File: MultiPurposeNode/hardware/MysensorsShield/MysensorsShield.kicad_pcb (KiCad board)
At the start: 2 copper layers, 20 parts, among them J1 IR RECEIVER, J2 TEMP SENSOR, J3 RADIO1, J4 RADIO2, J5 STEMMA, Q1 2N3904, U1 NRF24L01_Breakout

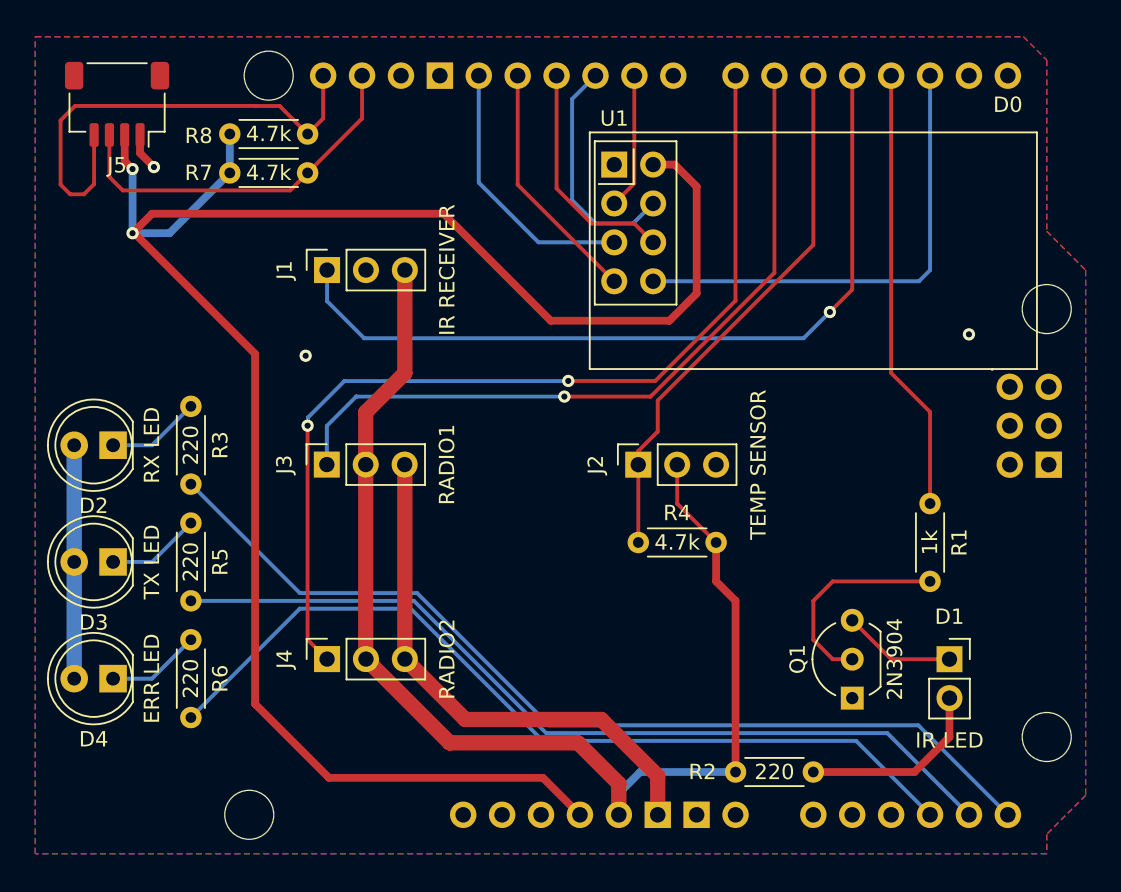
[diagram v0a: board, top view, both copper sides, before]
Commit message: MultiPurposeNode Rev.1 shield complete
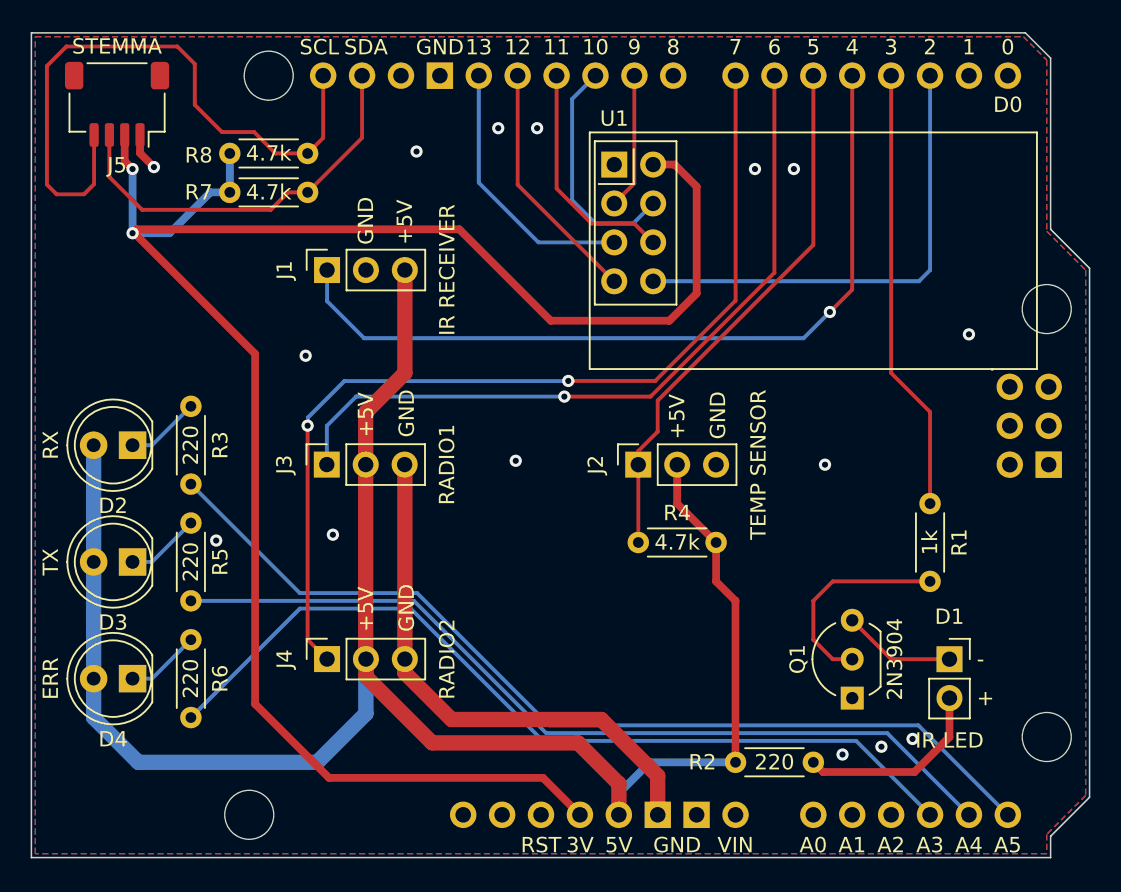
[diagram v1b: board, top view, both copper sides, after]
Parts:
- D2: value RX LED -> RX
- D3: value TX LED -> TX
- D4: value ERR LED -> ERR
- moved D2 1.27 mm to (71.1, 57.1)
- moved D3 1.27 mm to (71.1, 64.8)
- moved D4 1.27 mm to (71.1, 72.4)
- moved R7 1.27 mm to (77.5, 40.6)
- moved R8 1.27 mm to (77.5, 38.1)
- moved R2 0.64 mm to (110.5, 77.9)
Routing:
- net +5V: track 94.9 -> 121.6 mm
- net SCL: track 31.6 -> 42.1 mm
- net SDA: track 24.3 -> 26.1 mm
- net +3.3V: track 126.9 -> 125.5 mm
- net Net-(D4-K): track 6.13 -> 4.86 mm
- net Net-(D3-K): track 6.13 -> 4.86 mm
- net Net-(D2-K): track 6.13 -> 4.86 mm
- net GND: track 37.4 -> 37.9 mm, vias 3 -> 15
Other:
- board outline added: 69.1 x 53.8 mm
- board text added: "+"
- board text added: "+5V"
- board text added: "-"
- board text added: "0"
- board text added: "1"
- board text added: "10"
- board text added: "11"
- board text added: "12"
- board text added: "13"
- board text added: "2"
- board text added: "3"
- board text added: "3V"
- board text added: "4"
- board text added: "5"
- board text added: "5V"
- board text added: "6"
- board text added: "7"
- board text added: "8"
- board text added: "9"
- board text added: "A0"
- board text added: "A1"
- board text added: "A2"
- board text added: "A3"
- board text added: "A4"
- board text added: "A5"
- board text added: "GND"
- board text added: "RST"
- board text added: "SCL"
- board text added: "SDA"
- board text added: "VIN"
